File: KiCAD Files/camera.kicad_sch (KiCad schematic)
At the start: 2 parts, among them U1 K230_Rewired, U3 HC-FPC-0_5-22P-CXH20

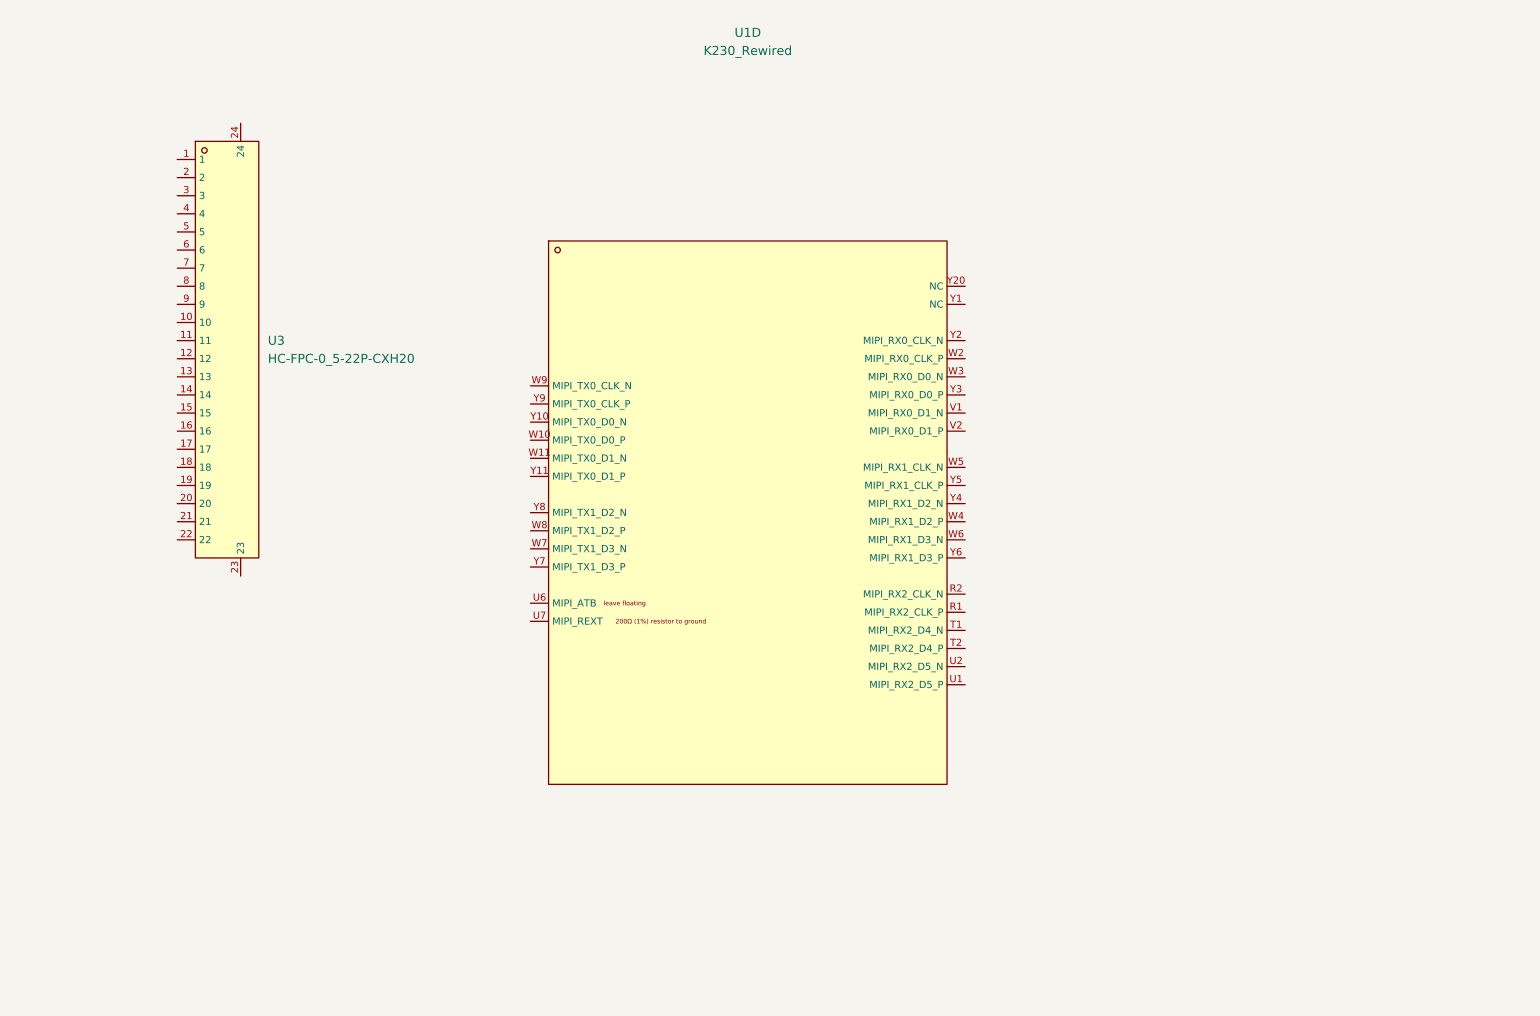
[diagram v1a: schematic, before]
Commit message: more peripherals
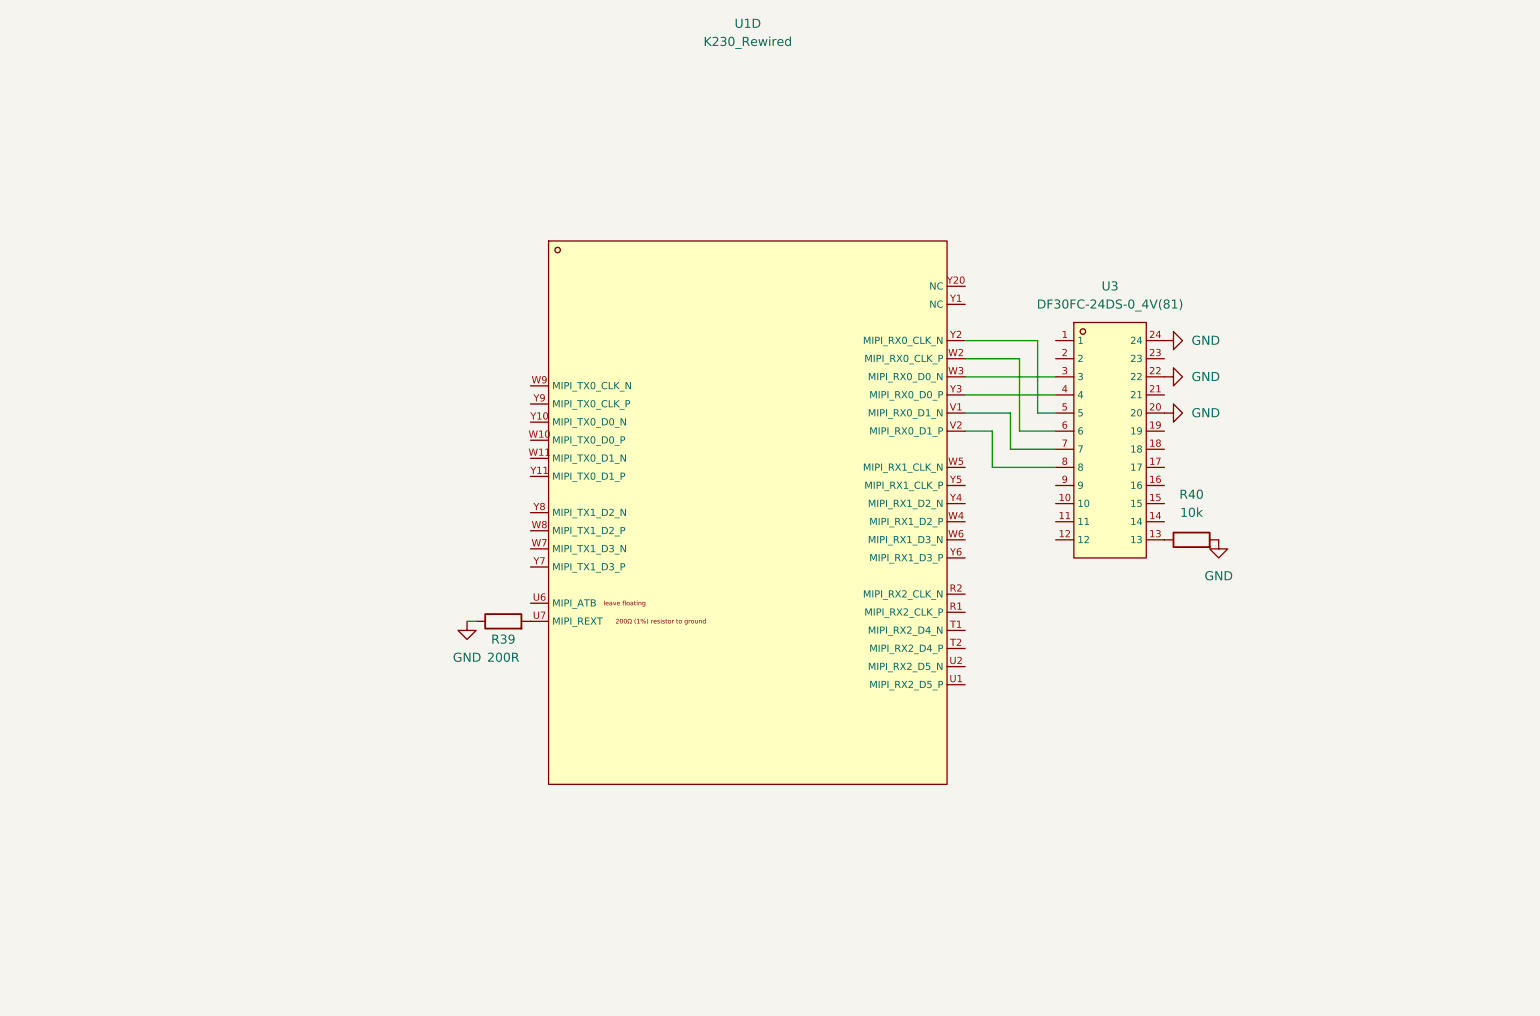
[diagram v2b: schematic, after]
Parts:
- removed U3: HC-FPC-0_5-22P-CXH20, footprints:FPC-SMD_22P-P0.50_HC-FPC-0.5-22P-CXH20, symbol LCSC:HC-FPC-0_5-22P-CXH20
- added R39: 200R, Resistor_SMD:R_0201_0603Metric, symbol Device:R
- added R40: 10k, Resistor_SMD:R_0402_1005Metric, symbol Device:R
- added U3: DF30FC-24DS-0_4V(81), footprints:CONN-SMD_DF30FC-24DS-0.4V-82, symbol LCSC:DF30FC-24DS-0_4V(81)
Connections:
- net at U1.U7 (MIPI_REXT): now also R39.2
- net at U1.V1 (MIPI_RX0_D1_N): now also U3.7
- net at U1.V2 (MIPI_RX0_D1_P): now also U3.8
- net at U1.W2 (MIPI_RX0_CLK_P): now also U3.6
- net at U1.W3 (MIPI_RX0_D0_N): now also U3.3
- net at U1.Y2 (MIPI_RX0_CLK_N): now also U3.5
- net at U1.Y3 (MIPI_RX0_D0_P): now also U3.4
- new net: R40.1, U3.13
- new net GND: R39.1, R40.2, U3.20, U3.22, U3.24

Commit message: schematic is pretty much done
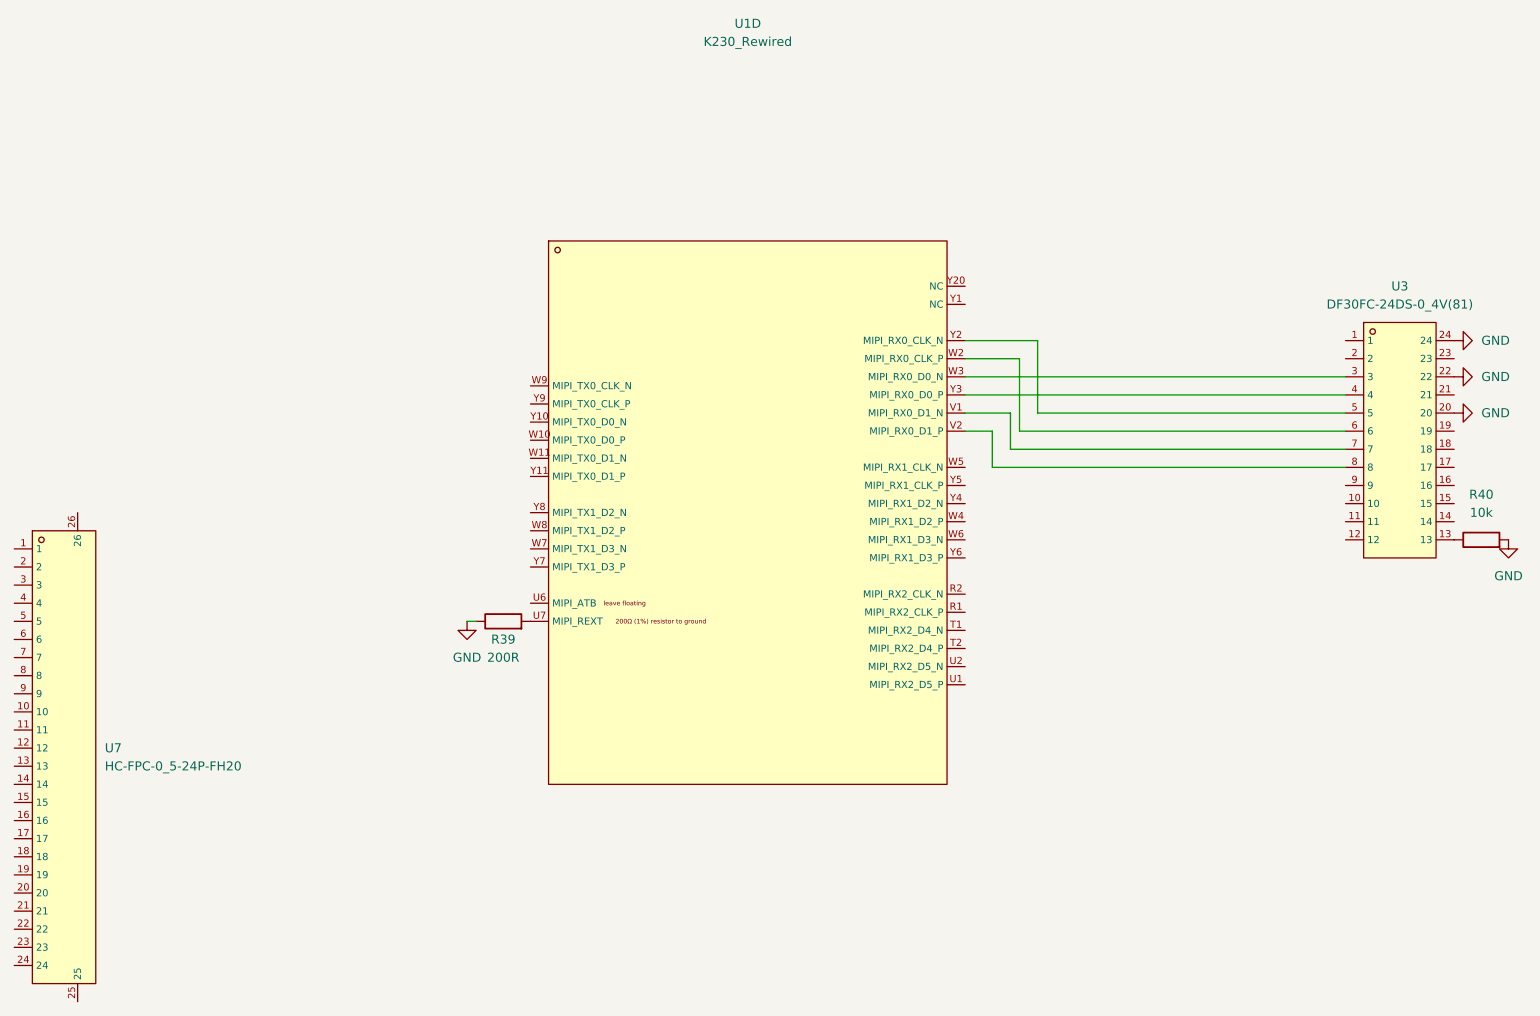
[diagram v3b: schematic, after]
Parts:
- added U7: HC-FPC-0_5-24P-FH20, footprints:FPC-SMD_24P-P0.50_HC-FPC-0.5-24P-FH20, symbol LCSC:HC-FPC-0_5-24P-FH20
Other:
- moved on the sheet: R40, U3
